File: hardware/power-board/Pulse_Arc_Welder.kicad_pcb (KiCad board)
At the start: 2 copper layers, 29 x 54.5 mm, 16 parts, among them J1 Conn_01x04_Male, J2 Conn_01x01, J3 Conn_01x01, J4 Conn_01x01, Q1 Q_NJFET_SGD, Q2 Q_NJFET_SGD, Q3 Q_NJFET_SGD, Q4 Q_NJFET_SGD

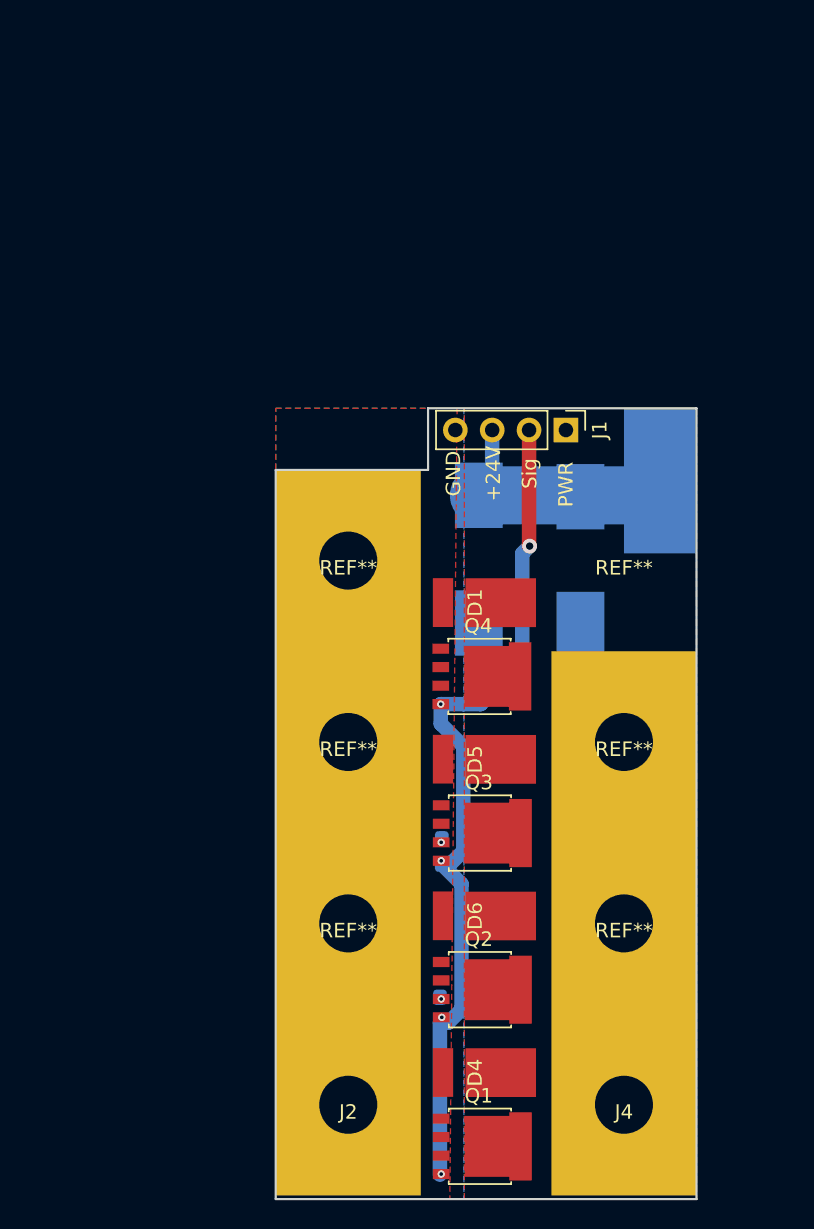
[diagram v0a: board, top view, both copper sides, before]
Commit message: Begun work on power board r.3
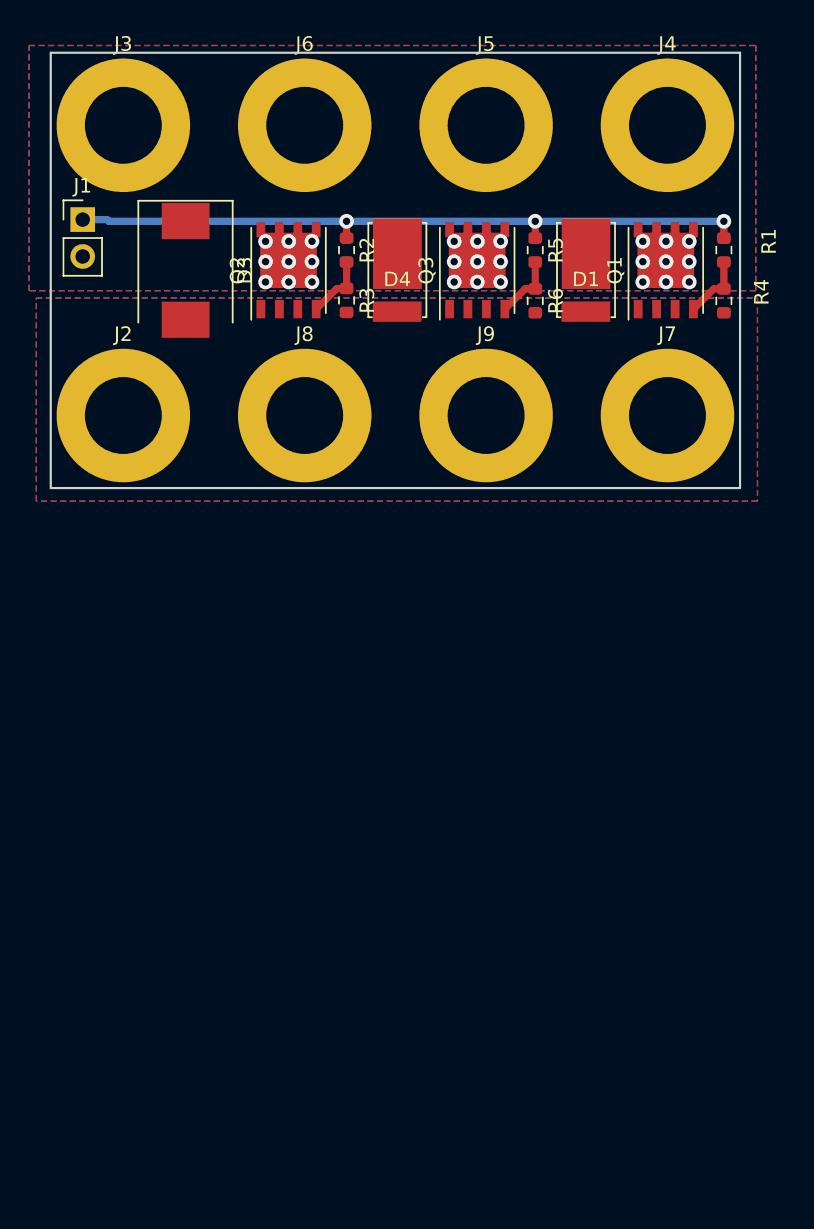
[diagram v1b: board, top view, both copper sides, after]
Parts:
- removed D2: 24V, Diode_SMD:D_SMC_Handsoldering
- removed D5, D6: D_Schottky_Small, pawelder:powerdi5
- removed Q4: Q_NJFET_SGD, Package_TO_SOT_SMD:LFPAK56
- added J5: Electrode, MountingHole:MountingHole_5.3mm_M5_DIN965_Pad, F.Cu at (142.5, 119.5)
- added J6: Electrode, MountingHole:MountingHole_5.3mm_M5_DIN965_Pad, F.Cu at (130.0, 119.5)
- added J7: BAT-, MountingHole:MountingHole_5.3mm_M5_DIN965_Pad, F.Cu at (155.0, 139.5)
- added J8: BAT-, MountingHole:MountingHole_5.3mm_M5_DIN965_Pad, F.Cu at (130.0, 139.5)
- added J9: BAT-, MountingHole:MountingHole_5.3mm_M5_DIN965_Pad, F.Cu at (142.5, 139.5)
- added R1: 10R, Resistor_SMD:R_0603_1608Metric, F.Cu at (158.9, 128.1)
- added R2: 10R, Resistor_SMD:R_0603_1608Metric, F.Cu at (132.9, 128.1)
- added R5: 10R, Resistor_SMD:R_0603_1608Metric, F.Cu at (145.9, 128.1)
- added R6: 10k, Resistor_SMD:R_0603_1608Metric, F.Cu at (145.9, 131.6)
- D1, D4: value D_Schottky_Small -> SBR10U45SP5
- D3: footprint Diode_SMD:D_SMC_Handsoldering -> Diode_SMD:D_SMC; moved to F.Cu
- J1: value Conn_01x04_Male -> to logic board; footprint Connector_PinHeader_2.54mm:PinHeader_1x04_P2.54mm_Vertical -> Connector_PinHeader_2.54mm:PinHeader_1x02_P2.54mm_Vertical
- J2: value Conn_01x01 -> BAT-; footprint pawelder:Bar connectorbig -> MountingHole:MountingHole_5.3mm_M5_DIN965_Pad
- J3: value Conn_01x01 -> Electrode; footprint Connector_Wire:SolderWirePad_1x01_SMD_5x10mm -> MountingHole:MountingHole_5.3mm_M5_DIN965_Pad; moved to F.Cu
- J4: value Conn_01x01 -> Electrode; footprint pawelder:Bar connector -> MountingHole:MountingHole_5.3mm_M5_DIN965_Pad
- Q1, Q2, Q3: value Q_NJFET_SGD -> SIR500DP-T1-RE3; footprint Package_TO_SOT_SMD:LFPAK56 -> Package_SO:PowerPAK_SO-8_Single
- R3, R4: footprint Resistor_SMD:R_0603_1608Metric_Pad1.05x0.95mm_HandSolder -> Resistor_SMD:R_0603_1608Metric; moved to F.Cu
- moved J4 67.6 mm to (155.0, 119.5)
- moved Q1 61.7 mm to (154.9, 129.5), turned to 90 degrees
- moved D4 55.5 mm to (136.4, 129.6), turned to 0 degrees
- moved R4 52.6 mm to (158.9, 131.6), turned to -90 degrees
- moved Q2 51.3 mm to (128.9, 129.5), turned to 90 degrees
- moved J2 50.0 mm to (117.5, 139.5)
- moved J3 44.4 mm to (117.5, 119.5), turned to 0 degrees
- moved Q3 38.8 mm to (141.9, 129.5), turned to 90 degrees
- moved R3 38.5 mm to (132.9, 131.6), turned to -90 degrees
- moved J1 36.3 mm to (114.7, 126.0), turned to 0 degrees
- moved D3 33.8 mm to (121.8, 129.5)
- moved D1 23.9 mm to (149.4, 129.6), turned to 0 degrees
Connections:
- D1 pad 1: PWR -> Electrode
- D3 pad 1: +24V -> Electrode
- D3 pad 2: PWR -> GND
- D4 pad 1: PWR -> Electrode
- J1 pad 1: PWR -> SIG
- J1 pad 2: SIG -> Electrode
- J3 pad 1: +24V -> Electrode
- J4 pad 1: PWR -> Electrode
- Q1 pad 4: SIG -> Net-(R4-Pad1)
- Q1 pad 5: PWR -> Electrode
- Q2 pad 4: SIG -> Net-(Q2-Pad4)
- Q2 pad 5: PWR -> Electrode
- Q3 pad 4: SIG -> Net-(Q3-Pad4)
- Q3 pad 5: PWR -> Electrode
- R3 pad 1: SIG -> Net-(Q2-Pad4)
- R4 pad 1: SIG -> Net-(R4-Pad1)
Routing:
- net +24V: track 17.7 -> 0.00 mm
- net SIG: track 58.6 -> 47.7 mm, vias 5 -> 3
- net Net-(R4-Pad1): track 0.00 -> 4.52 mm
- net Net-(Q3-Pad4): track 0.00 -> 4.52 mm
- net Net-(Q2-Pad4): track 0.00 -> 4.51 mm
- net GND: vias 2 -> 0
- net Electrode: vias 0 -> 27
- added copper zone on B.Cu, net Electrode
- added copper zone on F.Cu, net Electrode
- removed copper zone on B.Cu, net PWR
- removed copper zone on F.Cu, net PWR
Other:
- board size 29 x 54.5 mm -> 47.5 x 30 mm
- net class Default removed
- board text added: "ELEC"
- board text added: "ELECTRODE"
- board text added: "GNDPWR"
- board text added: "LGC BOARD"
- board text added: "WELD"
- board text added: "mad lightning stick"
- board text added: "pwr board r.3 benjamin hab"
- board text removed: "+24V"
- board text removed: "GND"
- board text removed: "PWR"
- board text removed: "Sig"
- board text removed: "pawelder r.1"
